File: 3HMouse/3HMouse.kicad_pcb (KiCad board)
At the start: 2 copper layers, 200 x 100 mm, 0 parts

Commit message: v0.1.0
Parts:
- added Brd1: SSD1306, SSD1306:128x64OLED, F.Cu at (215.1, 60.3)
- added C1: 22pF, Capacitor_SMD:C_0805_2012Metric, F.Cu at (160.5, 75.4)
- added C2: 22pF, Capacitor_SMD:C_0805_2012Metric, F.Cu at (147.5, 75.4)
- added C3: 0.1uF, Capacitor_SMD:C_0805_2012Metric, F.Cu at (150.6, 47.6)
- added C4: 0.1uF, Capacitor_SMD:C_0805_2012Metric, F.Cu at (142.9, 57.1)
- added C5: 0.1uF, Capacitor_SMD:C_0805_2012Metric, F.Cu at (167.5, 70.6)
- added C6: 0.1uF, Capacitor_SMD:C_0805_2012Metric, F.Cu at (154.8, 47.6)
- added C7: 10uF, Capacitor_SMD:C_0805_2012Metric, F.Cu at (138.1, 44.5)
- added C8: 1uF, Capacitor_SMD:C_0805_2012Metric, F.Cu at (143.5, 62.2)
- added D1: D_Small, Diode_SMD:D_SOD-123, F.Cu at (36.5, 50.0)
- added D10: D_Small, Diode_SMD:D_SOD-123, F.Cu at (62.7, 131.0)
- added D11: D_Small, Diode_SMD:D_SOD-123, F.Cu at (74.6, 50.0)
- added D12: D_Small, Diode_SMD:D_SOD-123, F.Cu at (74.6, 69.1)
- added D13: D_Small, Diode_SMD:D_SOD-123, F.Cu at (74.6, 88.1)
- added D14: D_Small, Diode_SMD:D_SOD-123, F.Cu at (84.1, 111.9)
- added D15: D_Small, Diode_SMD:D_SOD-123, F.Cu at (84.1, 131.0)
- added D16: D_Small, Diode_SMD:D_SOD-123, F.Cu at (103.2, 111.9)
- added D17: D_Small, Diode_SMD:D_SOD-123, F.Cu at (103.2, 131.0)
- added D18: D_Small, Diode_SMD:D_SOD-123, F.Cu at (122.2, 111.9)
- added D19: D_Small, Diode_SMD:D_SOD-123, F.Cu at (122.2, 131.0)
- added D2: D_Small, Diode_SMD:D_SOD-123, F.Cu at (36.5, 69.1)
- added D20: D_Small, Diode_SMD:D_SOD-123, F.Cu at (141.3, 111.9)
- added D21: D_Small, Diode_SMD:D_SOD-123, F.Cu at (141.3, 131.0)
- added D22: D_Small, Diode_SMD:D_SOD-123, F.Cu at (160.3, 111.9)
- added D23: D_Small, Diode_SMD:D_SOD-123, F.Cu at (160.3, 131.0)
- added D24: D_Small, Diode_SMD:D_SOD-123, F.Cu at (179.4, 111.9)
- added D25: D_Small, Diode_SMD:D_SOD-123, F.Cu at (179.4, 131.0)
- added D26: D_Small, Diode_SMD:D_SOD-123, F.Cu at (198.4, 111.9)
- added D27: D_Small, Diode_SMD:D_SOD-123, F.Cu at (198.4, 131.0)
- added D28: D_Small, Diode_SMD:D_SOD-123, F.Cu at (217.5, 111.9)
- added D29: D_Small, Diode_SMD:D_SOD-123, F.Cu at (217.4, 131.0)
- added D3: D_Small, Diode_SMD:D_SOD-123, F.Cu at (36.5, 88.1)
- added D4: D_Small, Diode_SMD:D_SOD-123, F.Cu at (41.3, 111.9)
- added D5: D_Small, Diode_SMD:D_SOD-123, F.Cu at (38.9, 131.0)
- added D6: D_Small, Diode_SMD:D_SOD-123, F.Cu at (55.6, 50.0)
- added D7: D_Small, Diode_SMD:D_SOD-123, F.Cu at (55.6, 69.1)
- added D8: D_Small, Diode_SMD:D_SOD-123, F.Cu at (55.6, 88.1)
- added D9: D_Small, Diode_SMD:D_SOD-123, F.Cu at (65.1, 111.9)
- added J1: USB_C_Receptacle, Connector_USB:USB_C_Receptacle_Amphenol_12401548E4-2A, F.Cu at (103.2, 37.3)
- added R1: 22, Resistor_SMD:R_0805_2012Metric, F.Cu at (124.6, 40.5)
- added R2: 22, Resistor_SMD:R_0805_2012Metric, F.Cu at (124.6, 43.7)
- added R3: 5.1k, Resistor_SMD:R_0805_2012Metric, F.Cu at (103.2, 48.4)
- added R4: 5.1k, Resistor_SMD:R_0805_2012Metric, F.Cu at (108.0, 48.4)
- added R5: 10k, Resistor_SMD:R_0805_2012Metric, F.Cu at (167.5, 59.6)
- added R6: 10k, Resistor_SMD:R_0805_2012Metric, F.Cu at (147.6, 72.8)
- added S1: RKJXV122400R, SamacSys_Parts:RKJXV122400R, F.Cu at (134.0, 62.1)
- added SW1: CherryMX, MX_Only:MXOnly-1U, F.Cu at (41.3, 41.3)
- added SW10: CherryMX, MX_Only:MXOnly-1U, F.Cu at (67.5, 122.2)
- added SW11: CherryMX, MX_Only:MXOnly-1U, F.Cu at (79.4, 41.3)
- added SW12: CherryMX, MX_Only:MXOnly-1U, F.Cu at (79.4, 60.3)
- added SW13: CherryMX, MX_Only:MXOnly-1U, F.Cu at (79.4, 79.4)
- added SW14: CherryMX, MX_Only:MXOnly-1U, F.Cu at (88.9, 103.2)
- added SW15: CherryMX, MX_Only:MXOnly-1U, F.Cu at (88.9, 122.2)
- added SW16: CherryMX, MX_Only:MXOnly-1U, F.Cu at (108.0, 103.2)
- added SW17: CherryMX, MX_Only:MXOnly-1U, F.Cu at (108.0, 122.2)
- added SW18: CherryMX, MX_Only:MXOnly-1U, F.Cu at (127.0, 103.2)
- added SW19: CherryMX, MX_Only:MXOnly-1U, F.Cu at (127.0, 122.2)
- added SW2: CherryMX, MX_Only:MXOnly-1U, F.Cu at (41.3, 60.3)
- added SW20: CherryMX, MX_Only:MXOnly-1U, F.Cu at (146.1, 103.2)
- added SW21: CherryMX, MX_Only:MXOnly-1U, F.Cu at (146.1, 122.2)
- added SW22: CherryMX, MX_Only:MXOnly-1U, F.Cu at (165.1, 103.2)
- added SW23: CherryMX, MX_Only:MXOnly-1U, F.Cu at (165.1, 122.2)
- added SW24: CherryMX, MX_Only:MXOnly-1U, F.Cu at (184.2, 103.2)
- added SW25: CherryMX, MX_Only:MXOnly-1U, F.Cu at (184.2, 122.2)
- added SW26: CherryMX, MX_Only:MXOnly-1U, F.Cu at (203.2, 103.2)
- added SW27: CherryMX, MX_Only:MXOnly-1U, F.Cu at (203.2, 122.2)
- added SW28: CherryMX, MX_Only:MXOnly-1U, F.Cu at (222.2, 103.2)
- added SW29: CherryMX, MX_Only:MXOnly-1U, F.Cu at (222.2, 122.2)
- added SW3: CherryMX, MX_Only:MXOnly-1U, F.Cu at (41.3, 79.4)
- added SW30: RotaryEncoder, Keebio-Parts:RotaryEncoder_EC11, F.Cu at (183.4, 72.2)
- added SW31: RotaryEncoder, Keebio-Parts:RotaryEncoder_EC11, F.Cu at (183.4, 47.6)
- added SW32: SW_Push, random-keyboard-parts:SKQG-1155865, F.Cu at (103.2, 79.4)
- added SW4: CherryMX, MX_Only:MXOnly-1U, F.Cu at (46.0, 103.2)
- added SW5: CherryMX, MX_Only:MXOnly-1U, F.Cu at (43.7, 122.2)
- added SW6: CherryMX, MX_Only:MXOnly-1U, F.Cu at (60.3, 41.3)
- added SW7: CherryMX, MX_Only:MXOnly-1U, F.Cu at (60.3, 60.3)
- added SW8: CherryMX, MX_Only:MXOnly-1U, F.Cu at (60.3, 79.4)
- added SW9: CherryMX, MX_Only:MXOnly-1U, F.Cu at (69.8, 103.2)
- added U1: AT90USB1286-A, Package_QFP:TQFP-64_14x14mm_P0.8mm, F.Cu at (155.6, 60.3)
- added Y1: 16 MHz, Crystal:Crystal_SMD_3225-4Pin_3.2x2.5mm, F.Cu at (154.6, 75.5)
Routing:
- net GND: track 0.00 -> 313.1 mm, vias 0 -> 9
- net ROW4: track 0.00 -> 265.8 mm, vias 0 -> 2
- net ROW3: track 0.00 -> 240.7 mm, vias 0 -> 20
- net COL0: track 0.00 -> 197.0 mm, vias 0 -> 1
- net +5V: track 0.00 -> 193.3 mm, vias 0 -> 6
- net COL1: track 0.00 -> 178.4 mm, vias 0 -> 1
- net ROW0: track 0.00 -> 176.5 mm, vias 0 -> 4
- net ROW2: track 0.00 -> 157.8 mm, vias 0 -> 6
- net COL2: track 0.00 -> 152.0 mm, vias 0 -> 2
- net ROW1: track 0.00 -> 139.1 mm, vias 0 -> 6
- net COL9: track 0.00 -> 103.8 mm
- net COL8: track 0.00 -> 84.2 mm
- net COL3: track 0.00 -> 70.9 mm, vias 0 -> 1
- net COL7: track 0.00 -> 64.9 mm
- net COL4: track 0.00 -> 59.7 mm, vias 0 -> 1
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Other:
- board size 200 x 100 mm -> 204.8 x 104.8 mm
- board text added: "JLCJLCJLCJLC"

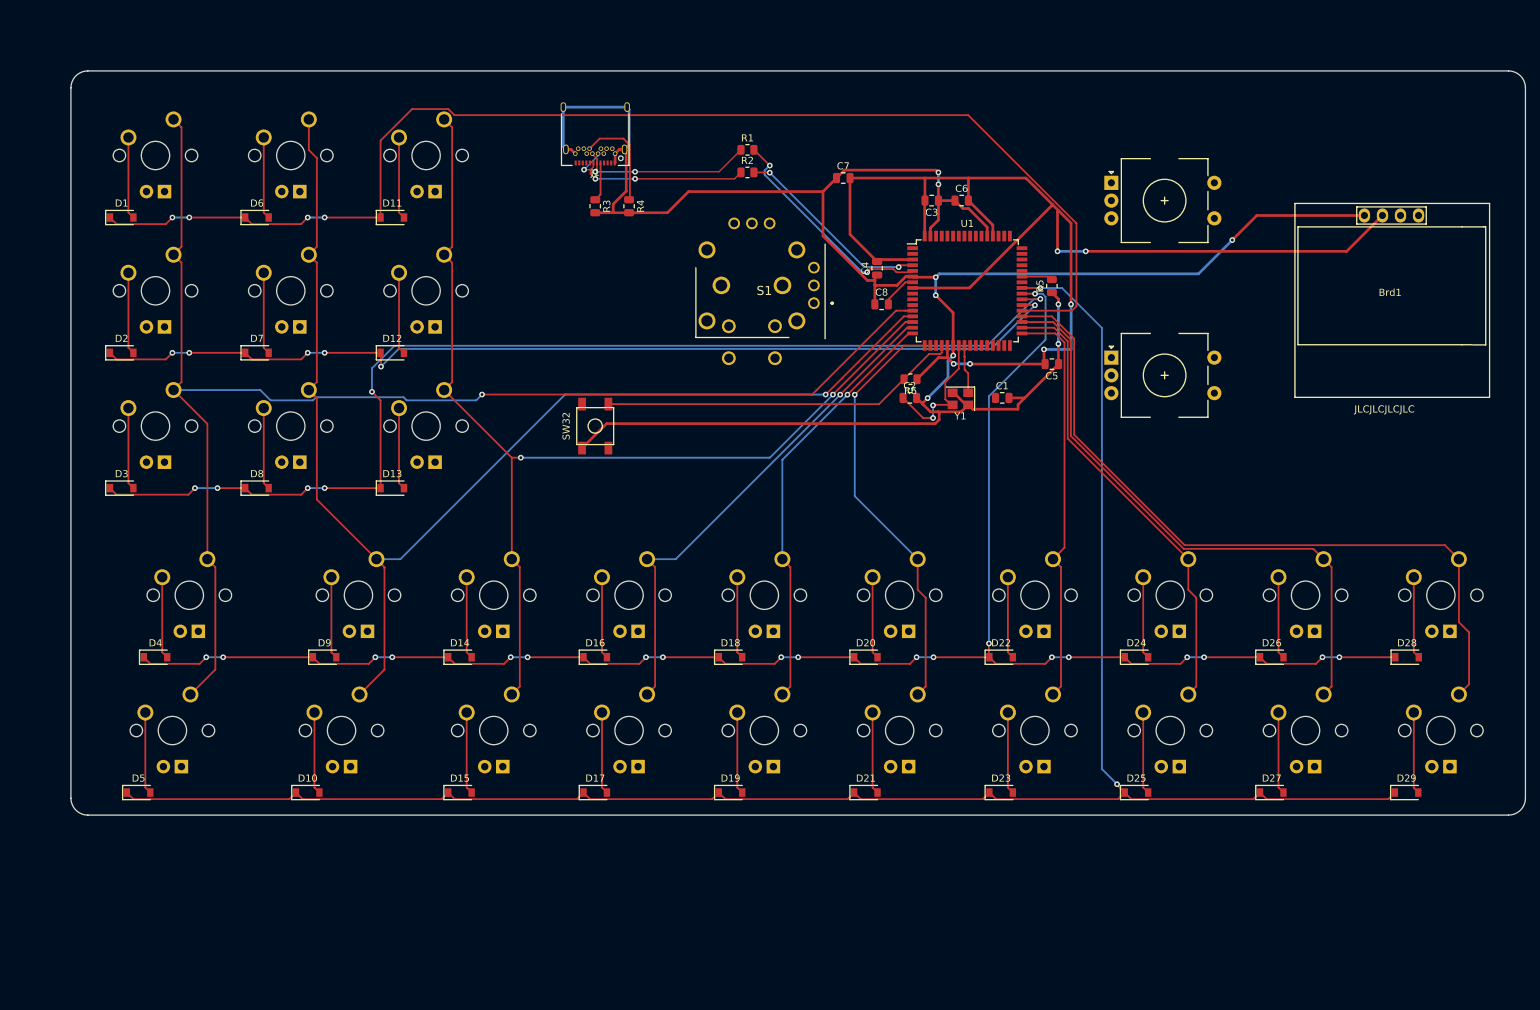
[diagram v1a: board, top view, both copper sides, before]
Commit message: Added ESD Protection and wired Joystick and Encoders
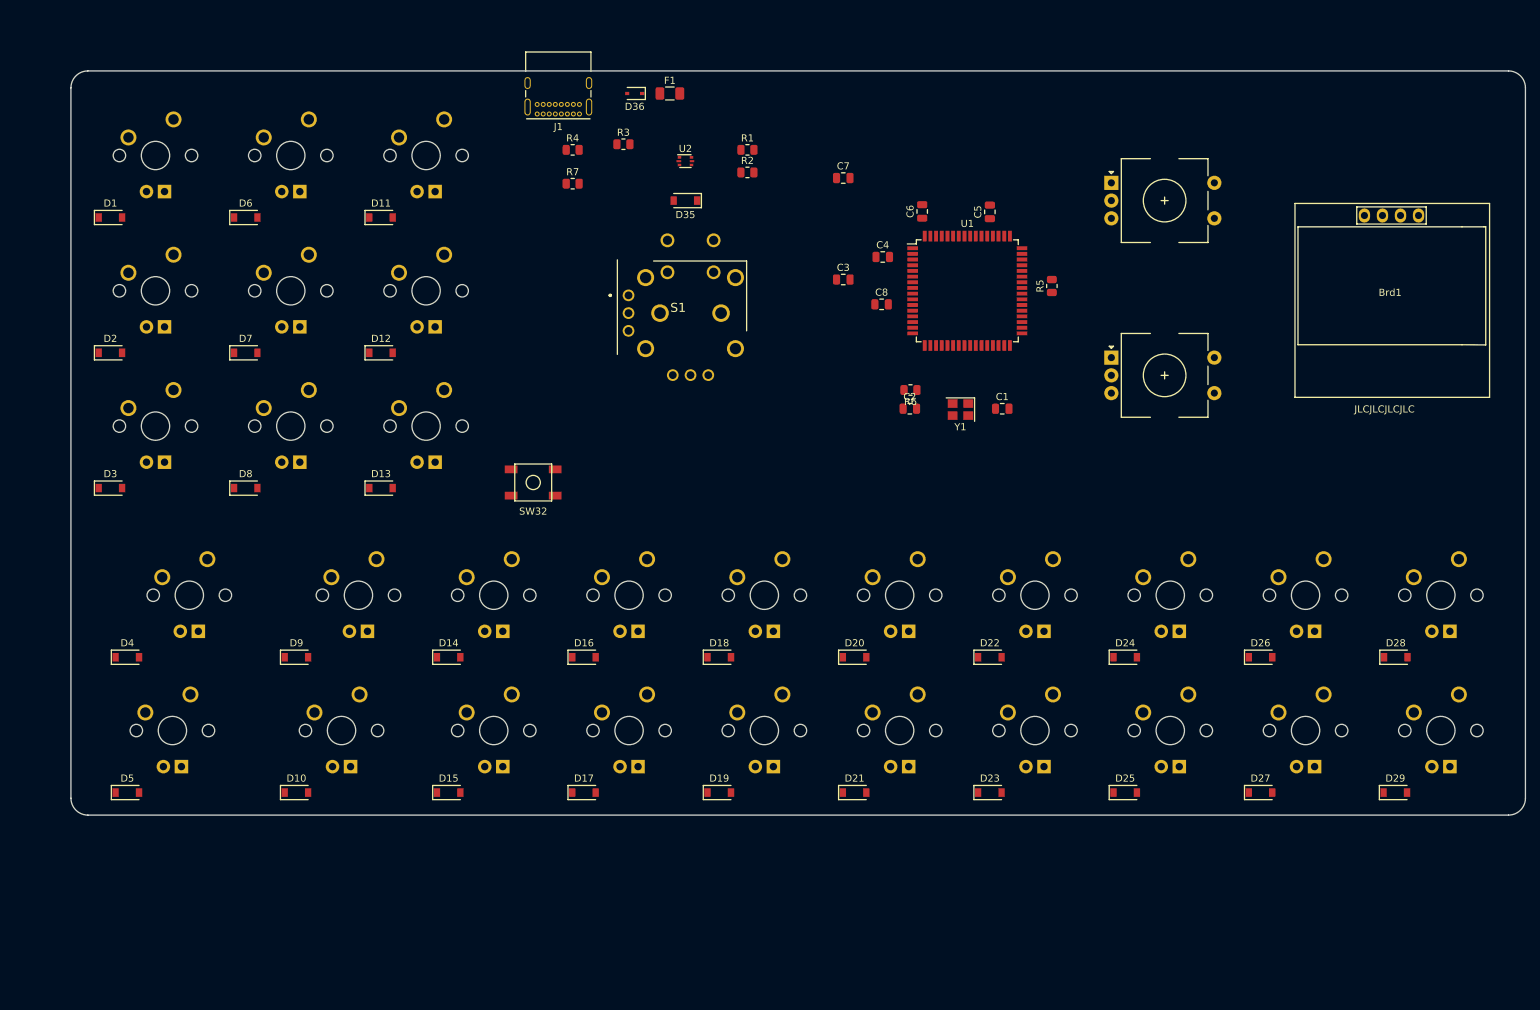
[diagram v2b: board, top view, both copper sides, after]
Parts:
- added D35: D_Small, Diode_SMD:D_SOD-123, F.Cu at (115.9, 47.6)
- added D36: SD05_SOD323, Diode_SMD:D_SOD-323, F.Cu at (108.7, 32.5)
- added F1: 500mA, Fuse:Fuse_1206_3216Metric, F.Cu at (113.7, 32.5)
- added R7: 5.1k, Resistor_SMD:R_0805_2012Metric, F.Cu at (100.0, 45.2)
- added U2: USBLC6-2P6, Package_TO_SOT_SMD:SOT-666, F.Cu at (115.9, 42.1)
- J1: value USB_C_Receptacle -> USB_C_Receptacle_USB2.0; footprint Connector_USB:USB_C_Receptacle_Amphenol_12401548E4-2A -> Connector_USB:USB_C_Receptacle_GCT_USB4085
- R3: value 5.1k -> 1M
- SW32: value SW_Push -> Reset
- moved S1 26.1 mm to (107.9, 61.0), turned to 180 degrees
- moved C5 23.1 mm to (158.8, 49.2), turned to 90 degrees
- moved C3 16.7 mm to (138.1, 58.7), turned to 0 degrees
- moved SW32 11.8 mm to (94.5, 87.3), turned to 0 degrees
- moved R4 11.2 mm to (100.0, 40.5), turned to 0 degrees
- moved R3 9.59 mm to (107.2, 39.7), turned to 0 degrees
- moved C6 5.76 mm to (149.2, 49.1), turned to 90 degrees
- moved D9 3.97 mm to (61.1, 111.9)
- moved D4 3.97 mm to (37.3, 111.9)
- moved J1 2.91 mm to (101.0, 35.4)
- moved C4 1.77 mm to (143.7, 55.6), turned to 0 degrees
- moved D1 1.59 mm to (34.9, 50.0)
- moved D14 1.59 mm to (82.5, 111.9)
- moved D15 1.59 mm to (82.5, 131.0)
- moved D16 1.59 mm to (101.6, 111.9)
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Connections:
- net VBUS renamed Net-(D36-Pad1)
- Brd1 pad 3: unconnected-(Brd1-Pad3) -> SCL
- Brd1 pad 4: unconnected-(Brd1-Pad4) -> SDA
- C3 pad 1: GND -> Net-(U1-Pad8)
- C4 pad 1: GND -> Net-(U1-Pad3)
- C5 pad 1: GND -> Net-(U1-Pad21)
- C6 pad 1: GND -> Net-(U1-Pad64)
- J1 pad A5: CC1 -> Net-(J1-PadA5)
- J1 pad A6: D+ -> D+ I
- J1 pad A7: D- -> D- I
- J1 pad B5: CC2 -> Net-(J1-PadB5)
- J1 pad B6: D+ -> D+ I
- J1 pad B7: D- -> D- I
- J1 pad S1: GND -> Net-(J1-PadS1)
- R3 pad 1: CC1 -> Net-(J1-PadS1)
- R4 pad 1: CC2 -> Net-(J1-PadA5)
- S1 pad A11: unconnected-(S1-PadA11) -> +5V
- S1 pad A12: unconnected-(S1-PadA12) -> VER
- S1 pad A13: unconnected-(S1-PadA13) -> GND
- S1 pad B11: unconnected-(S1-PadB11) -> +5V
- S1 pad B12: unconnected-(S1-PadB12) -> HOR
- S1 pad B13: unconnected-(S1-PadB13) -> GND
- S1 pad C1: unconnected-(S1-PadC1) -> COL10
- S1 pad D1: unconnected-(S1-PadD1) -> Net-(S1-PadD1)
- SW30 pad A: unconnected-(SW30-PadA) -> RE0A
- SW30 pad B: unconnected-(SW30-PadB) -> RE0B
- SW30 pad C: unconnected-(SW30-PadC) -> GND
- SW31 pad A: unconnected-(SW31-PadA) -> RE1A
- SW31 pad B: unconnected-(SW31-PadB) -> RE1B
- SW31 pad C: unconnected-(SW31-PadC) -> GND
- U1 pad 1: unconnected-(U1-Pad1) -> RE1A
- U1 pad 18: unconnected-(U1-Pad18) -> RE0A
- U1 pad 19: unconnected-(U1-Pad19) -> RE0B
- U1 pad 2: unconnected-(U1-Pad2) -> RE1B
- U1 pad 21: +5V -> Net-(U1-Pad21)
- U1 pad 25: unconnected-(U1-Pad25) -> SCL
- U1 pad 26: unconnected-(U1-Pad26) -> SDA
- U1 pad 3: +5V -> Net-(U1-Pad3)
- U1 pad 52: +5V -> Net-(U1-Pad21)
- U1 pad 60: unconnected-(U1-Pad60) -> HOR
- U1 pad 61: unconnected-(U1-Pad61) -> VER
- U1 pad 64: +5V -> Net-(U1-Pad64)
- U1 pad 8: +5V -> Net-(U1-Pad8)
- U1 pad 9: unconnected-(U1-Pad9) -> COL10
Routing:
- net GND: track 313.1 -> 0.00 mm, vias 9 -> 0
- net ROW4: track 265.8 -> 0.00 mm, vias 2 -> 0
- net ROW3: track 240.7 -> 0.00 mm, vias 20 -> 0
- net COL0: track 197.0 -> 0.00 mm, vias 1 -> 0
- net +5V: track 193.3 -> 0.00 mm, vias 6 -> 0
- net COL1: track 178.4 -> 0.00 mm, vias 1 -> 0
- net ROW0: track 176.5 -> 0.00 mm, vias 4 -> 0
- net ROW2: track 157.8 -> 0.00 mm, vias 6 -> 0
- net COL2: track 152.0 -> 0.00 mm, vias 2 -> 0
- net ROW1: track 139.1 -> 0.00 mm, vias 6 -> 0
- net COL9: track 103.8 -> 0.00 mm
- net COL8: track 84.2 -> 0.00 mm
- net COL3: track 70.9 -> 0.00 mm, vias 1 -> 0
- net COL7: track 64.9 -> 0.00 mm
- net COL4: track 59.7 -> 0.00 mm, vias 1 -> 0
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
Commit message: Added NC to Schematic
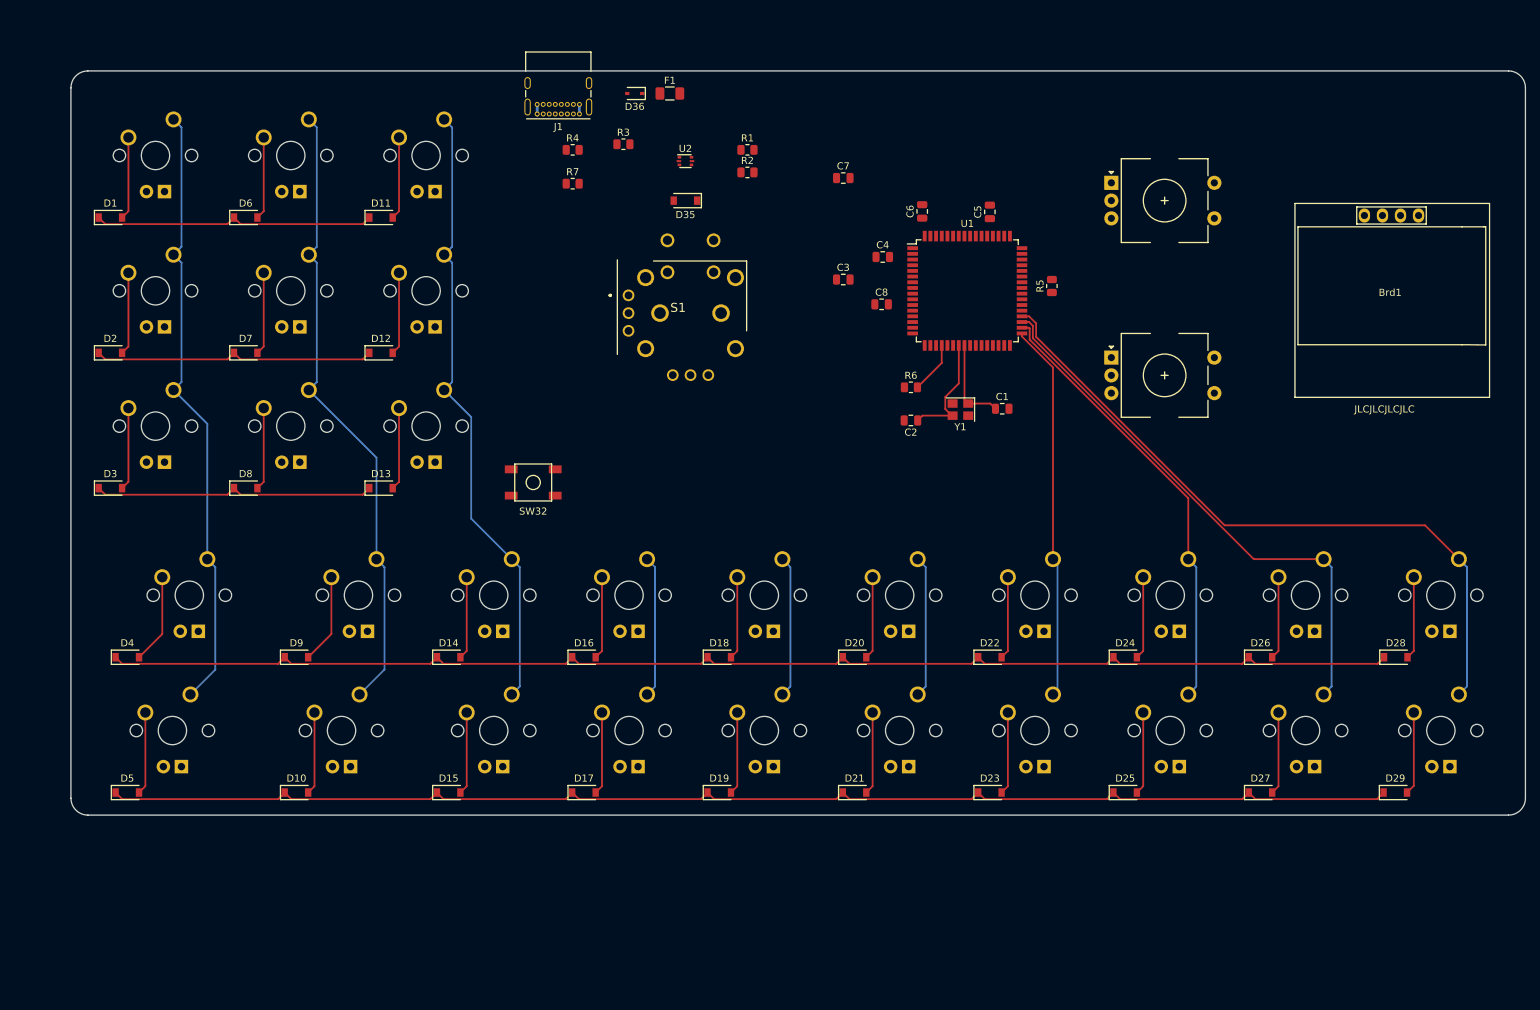
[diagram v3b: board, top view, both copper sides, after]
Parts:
- moved C2 1.66 mm to (147.6, 78.6), turned to 180 degrees
- moved R6 0.39 mm to (147.6, 73.9), turned to 0 degrees
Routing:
- net ROW3: track 0.00 -> 185.5 mm
- net ROW4: track 0.00 -> 185.4 mm
- net COL9: track 0.00 -> 96.8 mm
- net COL1: track 0.00 -> 88.7 mm
- net COL2: track 0.00 -> 87.7 mm
- net COL0: track 0.00 -> 86.7 mm
- net COL8: track 0.00 -> 77.3 mm
- net COL7: track 0.00 -> 62.9 mm
- net COL6: track 0.00 -> 53.2 mm
- net ROW0: track 0.00 -> 39.6 mm
- net ROW2: track 0.00 -> 39.6 mm
- net ROW1: track 0.00 -> 39.6 mm
- net COL5: track 0.00 -> 20.0 mm
- net COL4: track 0.00 -> 20.0 mm
- net COL3: track 0.00 -> 20.0 mm
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
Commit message: Finished Initial Routing
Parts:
- SW1, SW11, SW12, SW13, SW14, SW15, SW16, SW17, SW18, SW19, SW2, SW20, SW21, SW22, SW23, SW24, SW25, SW26, SW27, SW28, SW29, SW3, SW6, SW7, SW8, SW9: footprint MX_Only:MXOnly-1U -> MX_Only:MXOnly-1U-NoLED
- SW10, SW5: footprint MX_Only:MXOnly-1U -> MX_Only:MXOnly-1.25U-NoLED
- SW4: footprint MX_Only:MXOnly-1U -> MX_Only:MXOnly-1.5U-NoLED
- U2: value USBLC6-2P6 -> USBLC6-2SC6; footprint Package_TO_SOT_SMD:SOT-666 -> Package_TO_SOT_SMD:SOT-23-6
- moved C5 31.6 mm to (147.4, 78.7), turned to 180 degrees
- moved R1 7.78 mm to (124.7, 48.3)
- moved C8 7.69 mm to (139.6, 55.6)
- moved C2 6.61 mm to (153.4, 81.8), turned to -90 degrees
- moved C3 2.17 mm to (139.4, 60.5), turned to 180 degrees
- moved R5 1.75 mm to (166.2, 58.4), turned to 180 degrees
- moved C7 1.14 mm to (138.1, 43.3)
- moved C6 0.40 mm to (149.6, 49.3)
- moved U2 0.29 mm to (115.8, 41.8)
- moved C4 0.07 mm to (143.6, 55.6), turned to 180 degrees
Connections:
- U1 pad 1: RE1A -> unconnected-(U1-Pad1)
- U1 pad 18: RE0A -> unconnected-(U1-Pad18)
- U1 pad 19: RE0B -> unconnected-(U1-Pad19)
- U1 pad 2: RE1B -> unconnected-(U1-Pad2)
- U1 pad 25: SCL -> SDA
- U1 pad 26: SDA -> SCL
- U1 pad 37: ROW0 -> ROW2
- U1 pad 39: ROW2 -> ROW0
- U1 pad 45: unconnected-(U1-Pad45) -> RE0B
- U1 pad 46: unconnected-(U1-Pad46) -> RE0A
- U1 pad 47: unconnected-(U1-Pad47) -> RE1B
- U1 pad 48: unconnected-(U1-Pad48) -> RE1A
- U1 pad 60: HOR -> VER
- U1 pad 61: VER -> HOR
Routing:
- net +5V: track 0.00 -> 198.0 mm
- net COL0: track 86.7 -> 195.7 mm, vias 0 -> 5
- net ROW3: track 185.5 -> 292.2 mm, vias 0 -> 4
- net ROW1: track 39.6 -> 144.3 mm, vias 0 -> 2
- net ROW2: track 39.6 -> 143.8 mm, vias 0 -> 2
- net ROW0: track 39.6 -> 136.7 mm, vias 0 -> 2
- net GND: track 2.90 -> 91.5 mm, vias 0 -> 5
- net COL1: track 88.7 -> 174.7 mm, vias 0 -> 3
- net ROW4: track 185.4 -> 261.4 mm, vias 0 -> 2
- net COL2: track 87.7 -> 161.2 mm, vias 0 -> 1
- net SDA: track 0.00 -> 73.0 mm, vias 0 -> 1
- net SCL: track 0.00 -> 68.8 mm, vias 0 -> 1
- net Net-(R6-Pad2): track 7.31 -> 76.0 mm
- net VER: track 0.00 -> 56.8 mm, vias 0 -> 2
- net COL3: track 20.0 -> 74.2 mm, vias 0 -> 1
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- added copper zone on F.Cu, net GND
